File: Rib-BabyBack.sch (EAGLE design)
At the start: 27 parts, among them IC1 REG1117, SW1 DPDT

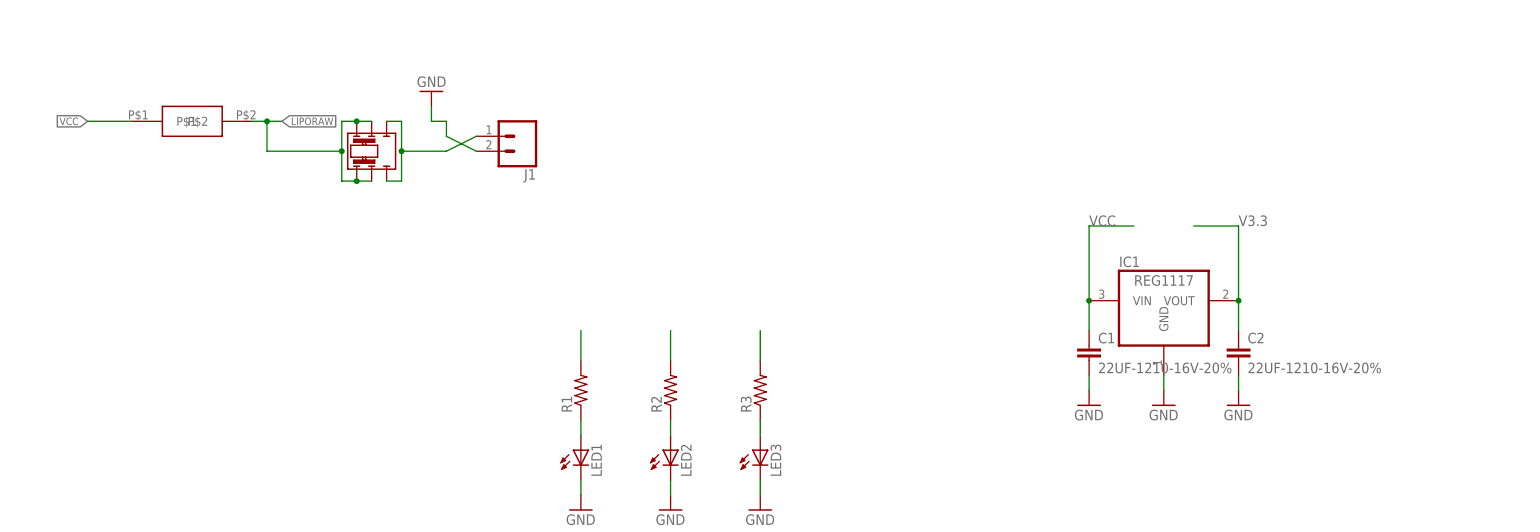
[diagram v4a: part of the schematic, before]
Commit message: Issue #21 Added a pad for a PTC resetabble fuse for the 3.3v rail
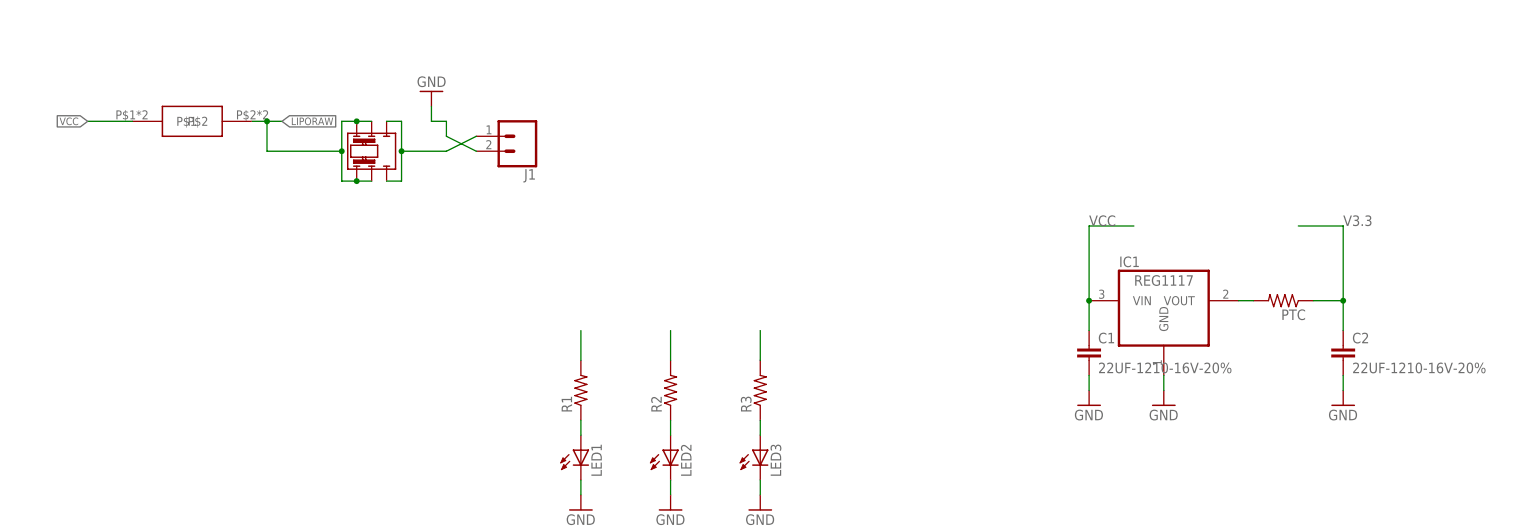
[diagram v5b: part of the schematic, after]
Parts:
- added PTC: (no value), resistor:R-US_R0805
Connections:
- new net N$7: IC1.VOUT, PTC.2
- net V3.3: now also PTC.1; no longer IC1.VOUT
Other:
- moved on the sheet: C2

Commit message: Issues #33 and 4 and #36
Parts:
- added JP9: (no value), jumper:JP2E
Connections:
- removed net V3.3: C2.1, JP2.19, JP3.19, JP4.1, JP4.10, JP4.11, JP4.12, JP4.13, JP4.14, JP4.15, JP4.16, JP4.17, JP4.18, JP4.19, JP4.2, JP4.3, JP4.4, JP4.5, JP4.6, JP4.7, JP4.8, JP4.9, JP6.19, PTC.1, R3.2, R5.1, R6.1, U$5.VCC
- new net 3V3: JP2.19, JP3.19, JP6.19, JP9.1, R5.1, R6.1, U$5.VCC
- new net SENSORV: JP4.1, JP4.10, JP4.11, JP4.12, JP4.13, JP4.14, JP4.15, JP4.16, JP4.17, JP4.18, JP4.19, JP4.2, JP4.3, JP4.4, JP4.5, JP4.6, JP4.7, JP4.8, JP4.9, JP9.2
- net 5V: now also C2.1, JP9.3, PTC.1, R3.2

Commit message: Issue #34
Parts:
- added D1: (no value), adafruit:DIODESOD-523
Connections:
- new net N$6: C2.1, D1.A, PTC.1
- net 5V: now also D1.C; no longer C2.1, PTC.1
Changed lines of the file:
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@@
 <part name="PTC" library="resistor" library_urn="urn:adsk.eagle:library:348" deviceset="R-US_" device="R0805" package3d_urn="urn:adsk.eagle:package:26059/1"/>
 <part name="JP9" library="jumper" library_urn="urn:adsk.eagle:library:252" deviceset="JP2E" device="" package3d_urn="urn:adsk.eagle:package:15452/1"/>
+<part name="D1" library="adafruit" deviceset="DIODE" device="SOD-523"/>
 </parts>
 <sheets>
@@
 <instance part="PTC" gate="G$1" x="215.9" y="-86.36" rot="R180"/>
 <instance part="JP9" gate="1" x="-78.74" y="-208.28"/>
+<instance part="D1" gate="G$1" x="231.14" y="-86.36"/>
 </instances>
 <busses>
@@
 </segment>
 <segment>
-<wire x1="218.44" y1="-73.66" x2="226.06" y2="-73.66" width="0.1524" layer="91"/>
 <label x="226.06" y="-73.66" size="1.778" layer="95"/>
-<pinref part="PTC" gate="G$1" pin="1"/>
-<wire x1="220.98" y1="-86.36" x2="226.06" y2="-86.36" width="0.1524" layer="91"/>
-<pinref part="C2" gate="G$1" pin="1"/>
-<wire x1="226.06" y1="-86.36" x2="226.06" y2="-91.44" width="0.1524" layer="91"/>
-<wire x1="226.06" y1="-73.66" x2="226.06" y2="-86.36" width="0.1524" layer="91"/>
-<junction x="226.06" y="-86.36"/>
+<pinref part="D1" gate="G$1" pin="C"/>
+<wire x1="233.68" y1="-86.36" x2="236.22" y2="-86.36" width="0.1524" layer="91"/>
+<wire x1="236.22" y1="-86.36" x2="236.22" y2="-73.66" width="0.1524" layer="91"/>
+<wire x1="236.22" y1="-73.66" x2="218.44" y2="-73.66" width="0.1524" layer="91"/>
 </segment>
 <segment>
@@
 </segment>
 </net>
+<net name="N$6" class="0">
+<segment>
+<pinref part="PTC" gate="G$1" pin="1"/>
+<pinref part="D1" gate="G$1" pin="A"/>
+<wire x1="220.98" y1="-86.36" x2="226.06" y2="-86.36" width="0.1524" layer="91"/>
+<pinref part="C2" gate="G$1" pin="1"/>
+<wire x1="226.06" y1="-86.36" x2="228.6" y2="-86.36" width="0.1524" layer="91"/>
+<wire x1="226.06" y1="-91.44" x2="226.06" y2="-86.36" width="0.1524" layer="91"/>
+<junction x="226.06" y="-86.36"/>
+</segment>
+</net>

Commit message: Resolved issue 37
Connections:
- net 5V: now also JP4.14, JP4.15, JP4.16, JP4.17, JP4.18, JP4.19
- net SENSORV: no longer JP4.14, JP4.15, JP4.16, JP4.17, JP4.18, JP4.19
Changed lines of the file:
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@@
 <wire x1="-76.2" y1="-210.82" x2="-76.2" y2="-215.9" width="0.1524" layer="91"/>
+</segment>
+<segment>
+<pinref part="JP4" gate="G$1" pin="15"/>
+<pinref part="JP4" gate="G$1" pin="19"/>
+<wire x1="-22.86" y1="-91.44" x2="-22.86" y2="-93.98" width="0.1524" layer="91"/>
+<wire x1="-22.86" y1="-93.98" x2="-22.86" y2="-96.52" width="0.1524" layer="91"/>
+<wire x1="-22.86" y1="-96.52" x2="-22.86" y2="-99.06" width="0.1524" layer="91"/>
+<wire x1="-22.86" y1="-99.06" x2="-22.86" y2="-101.6" width="0.1524" layer="91"/>
+<wire x1="-22.86" y1="-101.6" x2="-22.86" y2="-106.68" width="0.1524" layer="91"/>
+<junction x="-22.86" y="-101.6"/>
+<pinref part="JP4" gate="G$1" pin="16"/>
+<junction x="-22.86" y="-93.98"/>
+<pinref part="JP4" gate="G$1" pin="17"/>
+<junction x="-22.86" y="-96.52"/>
+<pinref part="JP4" gate="G$1" pin="18"/>
+<junction x="-22.86" y="-99.06"/>
+<pinref part="JP4" gate="G$1" pin="14"/>
+<wire x1="-22.86" y1="-88.9" x2="-22.86" y2="-91.44" width="0.1524" layer="91"/>
+<junction x="-22.86" y="-91.44"/>
 </segment>
 </net>
@@
 <pinref part="JP4" gate="G$1" pin="11"/>
 <label x="-22.86" y="-55.88" size="1.27" layer="95" rot="R180" xref="yes"/>
-<pinref part="JP4" gate="G$1" pin="19"/>
 <wire x1="-22.86" y1="-81.28" x2="-22.86" y2="-83.82" width="0.1524" layer="91"/>
 <junction x="-22.86" y="-81.28"/>
@@
 <junction x="-22.86" y="-83.82"/>
 <pinref part="JP4" gate="G$1" pin="13"/>
-<wire x1="-22.86" y1="-86.36" x2="-22.86" y2="-88.9" width="0.1524" layer="91"/>
-<junction x="-22.86" y="-86.36"/>
-<pinref part="JP4" gate="G$1" pin="14"/>
-<wire x1="-22.86" y1="-88.9" x2="-22.86" y2="-91.44" width="0.1524" layer="91"/>
-<junction x="-22.86" y="-88.9"/>
-<pinref part="JP4" gate="G$1" pin="15"/>
-<wire x1="-22.86" y1="-91.44" x2="-22.86" y2="-93.98" width="0.1524" layer="91"/>
-<junction x="-22.86" y="-91.44"/>
-<pinref part="JP4" gate="G$1" pin="16"/>
-<wire x1="-22.86" y1="-93.98" x2="-22.86" y2="-96.52" width="0.1524" layer="91"/>
-<junction x="-22.86" y="-93.98"/>
-<pinref part="JP4" gate="G$1" pin="17"/>
-<wire x1="-22.86" y1="-96.52" x2="-22.86" y2="-99.06" width="0.1524" layer="91"/>
-<junction x="-22.86" y="-96.52"/>
-<pinref part="JP4" gate="G$1" pin="18"/>
-<wire x1="-22.86" y1="-99.06" x2="-22.86" y2="-101.6" width="0.1524" layer="91"/>
-<junction x="-22.86" y="-99.06"/>
-</segment>
-<segment>
+</segment>
+<segment>
